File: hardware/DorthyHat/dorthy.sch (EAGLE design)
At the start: 25 parts, among them J1 90325-0004, J2 90325-0004, U2 DEV-15583

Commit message: added touch screen lcd to dorthy, realized teensy 4.0 does not have true analog outputs, need to revert to 3.5 if I want simple outs...
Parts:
- removed R7: 10k, rcl:R-US_R0805
- removed R8: 10K, rcl:R-US_R0805
- added R10, R11: 10K, rcl:R-US_0207/10
- added R9: 100, rcl:R-US_0207/10
- added SV7: (no value), con-lstb:MA04-1
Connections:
- new net LED: JP1.8, R9.2
- net GND: now also SV7.1
- net LA: no longer U2.15
- net RA: no longer U2.14
- net SCL: now also R10.2, SV7.4; no longer R7.2
- net SDA: now also R11.2, SV7.3; no longer R8.2
- net VCC: now also R9.1; no longer JP1.8
- net VEE: now also R10.1, R11.1, SV7.2; no longer R7.1, R8.1
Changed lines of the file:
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@@
 <part name="C3" library="capacitor-wima" library_urn="urn:adsk.eagle:library:116" deviceset="C" device="5/3.5" package3d_urn="urn:adsk.eagle:package:5427/1" value="1uf"/>
 <part name="U$7" library="seeedgrove" deviceset="110990030" device=""/>
-<part name="R7" library="rcl" library_urn="urn:adsk.eagle:library:334" deviceset="R-US_" device="R0805" package3d_urn="urn:adsk.eagle:package:23553/2" value="10k"/>
-<part name="R8" library="rcl" library_urn="urn:adsk.eagle:library:334" deviceset="R-US_" device="R0805" package3d_urn="urn:adsk.eagle:package:23553/2" value="10K"/>
 <part name="SV5" library="con-lstb" library_urn="urn:adsk.eagle:library:162" deviceset="MA04-1" device="" package3d_urn="urn:adsk.eagle:package:8337/1"/>
 <part name="SV2" library="con-lsta" library_urn="urn:adsk.eagle:library:161" deviceset="FE06-1" device="" package3d_urn="urn:adsk.eagle:package:8191/1"/>
@@
 <part name="U2" library="DEV-15583" deviceset="DEV-15583" device=""/>
 <part name="JP1" library="pinhead" library_urn="urn:adsk.eagle:library:325" deviceset="PINHD-1X14" device="" package3d_urn="urn:adsk.eagle:package:22417/2"/>
+<part name="R9" library="rcl" library_urn="urn:adsk.eagle:library:334" deviceset="R-US_" device="0207/10" package3d_urn="urn:adsk.eagle:package:23491/2" value="100"/>
+<part name="R10" library="rcl" library_urn="urn:adsk.eagle:library:334" deviceset="R-US_" device="0207/10" package3d_urn="urn:adsk.eagle:package:23491/2" value="10K"/>
+<part name="R11" library="rcl" library_urn="urn:adsk.eagle:library:334" deviceset="R-US_" device="0207/10" package3d_urn="urn:adsk.eagle:package:23491/2" value="10K"/>
+<part name="SV7" library="con-lstb" library_urn="urn:adsk.eagle:library:162" deviceset="MA04-1" device="" package3d_urn="urn:adsk.eagle:package:8337/1"/>
 </parts>
 <sheets>
@@
 <plain>
 <text x="157.48" y="81.28" size="1.778" layer="91">LCD Display</text>
-<text x="157.48" y="132.08" size="1.778" layer="91">Optional pullups, do not populate if not needed</text>
+<text x="154.94" y="134.62" size="1.778" layer="91">Optional pullups, do not populate if not needed</text>
 <text x="137.16" y="48.26" size="1.778" layer="91">Optional, connector if desired to go grove to grove. beware of orintation during install</text>
 <text x="-63.5" y="35.56" size="1.778" layer="91">MIDI THROUGH</text>
@@
 <attribute name="VALUE" x="162.56" y="71.12" size="1.27" layer="96"/>
 </instance>
-<instance part="R7" gate="G$1" x="177.8" y="127" smashed="yes">
-<attribute name="NAME" x="173.99" y="128.4986" size="1.778" layer="95"/>
-<attribute name="VALUE" x="173.99" y="123.698" size="1.778" layer="96"/>
-</instance>
-<instance part="R8" gate="G$1" x="177.8" y="119.38" smashed="yes">
-<attribute name="NAME" x="173.99" y="120.8786" size="1.778" layer="95"/>
-<attribute name="VALUE" x="173.99" y="116.078" size="1.778" layer="96"/>
-</instance>
 <instance part="SV5" gate="1" x="182.88" y="66.04" smashed="yes">
 <attribute name="VALUE" x="181.61" y="55.88" size="1.778" layer="96"/>
@@
 <attribute name="NAME" x="-52.07" y="145.415" size="1.778" layer="95"/>
 <attribute name="VALUE" x="-52.07" y="104.14" size="1.778" layer="96"/>
+</instance>
+<instance part="R9" gate="G$1" x="-114.3" y="121.92" smashed="yes">
+<attribute name="NAME" x="-113.03" y="125.9586" size="1.778" layer="95"/>
+<attribute name="VALUE" x="-113.03" y="123.698" size="1.778" layer="96"/>
+</instance>
+<instance part="R10" gate="G$1" x="177.8" y="127" smashed="yes">
+<attribute name="NAME" x="179.07" y="131.0386" size="1.778" layer="95"/>
+<attribute name="VALUE" x="179.07" y="128.778" size="1.778" layer="96"/>
+</instance>
+<instance part="R11" gate="G$1" x="177.8" y="119.38" smashed="yes">
+<attribute name="NAME" x="179.07" y="123.4186" size="1.778" layer="95"/>
+<attribute name="VALUE" x="179.07" y="121.158" size="1.778" layer="96"/>
+</instance>
+<instance part="SV7" gate="1" x="152.4" y="205.74" smashed="yes">
+<attribute name="VALUE" x="151.13" y="195.58" size="1.778" layer="96"/>
+<attribute name="NAME" x="151.13" y="211.582" size="1.778" layer="95"/>
 </instance>
 </instances>
@@
 </segment>
 <segment>
-<pinref part="JP1" gate="A" pin="8"/>
-<wire x1="-48.26" y1="124.46" x2="-60.96" y2="124.46" width="0.1524" layer="91"/>
-<label x="-60.96" y="124.46" size="1.778" layer="95"/>
+<pinref part="R9" gate="G$1" pin="1"/>
+<wire x1="-119.38" y1="121.92" x2="-129.54" y2="121.92" width="0.1524" layer="91"/>
+<label x="-127" y="121.92" size="1.778" layer="95"/>
 </segment>
 </net>
@@
 <wire x1="-48.26" y1="139.7" x2="-60.96" y2="139.7" width="0.1524" layer="91"/>
 <label x="-60.96" y="139.7" size="1.778" layer="95"/>
+</segment>
+<segment>
+<wire x1="177.8" y1="200.66" x2="160.02" y2="200.66" width="0.1524" layer="91"/>
+<label x="160.02" y="200.66" size="1.778" layer="95"/>
+<pinref part="SV7" gate="1" pin="1"/>
 </segment>
 </net>
@@
 <wire x1="167.64" y1="119.38" x2="172.72" y2="119.38" width="0.1524" layer="91"/>
 <label x="167.64" y="127" size="1.778" layer="95"/>
-<pinref part="R7" gate="G$1" pin="1"/>
-<pinref part="R8" gate="G$1" pin="1"/>
+<pinref part="R11" gate="G$1" pin="1"/>
+<pinref part="R10" gate="G$1" pin="1"/>
 </segment>
 <segment>
@@
 <label x="-60.96" y="134.62" size="1.778" layer="95"/>
 </segment>
+<segment>
+<wire x1="177.8" y1="203.2" x2="160.02" y2="203.2" width="0.1524" layer="91"/>
+<label x="160.02" y="203.2" size="1.778" layer="95"/>
+<pinref part="SV7" gate="1" pin="2"/>
+</segment>
 </net>
 <net name="RXBUF" class="0">
@@
 <wire x1="182.88" y1="127" x2="190.5" y2="127" width="0.1524" layer="91"/>
 <label x="185.42" y="127" size="1.778" layer="95"/>
-<pinref part="R7" gate="G$1" pin="2"/>
+<pinref part="R10" gate="G$1" pin="2"/>
 </segment>
 <segment>
@@
 <pinref part="U2" gate="G$1" pin="19"/>
 </segment>
+<segment>
+<wire x1="177.8" y1="208.28" x2="160.02" y2="208.28" width="0.1524" layer="91"/>
+<label x="160.02" y="208.28" size="1.778" layer="95"/>
+<pinref part="SV7" gate="1" pin="4"/>
+</segment>
 </net>
 <net name="SDA" class="0">
@@
 <wire x1="182.88" y1="119.38" x2="190.5" y2="119.38" width="0.1524" layer="91"/>
 <label x="185.42" y="119.38" size="1.778" layer="95"/>
-<pinref part="R8" gate="G$1" pin="2"/>
+<pinref part="R11" gate="G$1" pin="2"/>
 </segment>
 <segment>
@@
 <pinref part="U2" gate="G$1" pin="18"/>
 </segment>
+<segment>
+<wire x1="177.8" y1="205.74" x2="160.02" y2="205.74" width="0.1524" layer="91"/>
+<label x="160.02" y="205.74" size="1.778" layer="95"/>
+<pinref part="SV7" gate="1" pin="3"/>
+</segment>
 </net>
 <net name="MIDITX" class="0">
@@
 </segment>
 <segment>
-<wire x1="33.02" y1="121.92" x2="43.18" y2="121.92" width="0.1524" layer="91"/>
-<label x="35.56" y="121.92" size="1.778" layer="95"/>
-<pinref part="U2" gate="G$1" pin="15"/>
+<wire x1="12.7" y1="160.02" x2="22.86" y2="160.02" width="0.1524" layer="91"/>
+<label x="15.24" y="160.02" size="1.778" layer="95"/>
 </segment>
 </net>
@@
 </segment>
 <segment>
-<wire x1="33.02" y1="119.38" x2="43.18" y2="119.38" width="0.1524" layer="91"/>
-<label x="35.56" y="119.38" size="1.778" layer="95"/>
-<pinref part="U2" gate="G$1" pin="14"/>
+<wire x1="12.7" y1="157.48" x2="22.86" y2="157.48" width="0.1524" layer="91"/>
+<label x="15.24" y="157.48" size="1.778" layer="95"/>
 </segment>
 </net>
@@
 </segment>
 </net>
+<net name="LED" class="0">
+<segment>
+<pinref part="JP1" gate="A" pin="8"/>
+<wire x1="-48.26" y1="124.46" x2="-60.96" y2="124.46" width="0.1524" layer="91"/>
+<label x="-60.96" y="124.46" size="1.778" layer="95"/>
+</segment>
+<segment>
+<pinref part="R9" gate="G$1" pin="2"/>
+<wire x1="-109.22" y1="121.92" x2="-96.52" y2="121.92" width="0.1524" layer="91"/>
+<label x="-106.68" y="121.92" size="1.778" layer="95"/>
+</segment>
+</net>

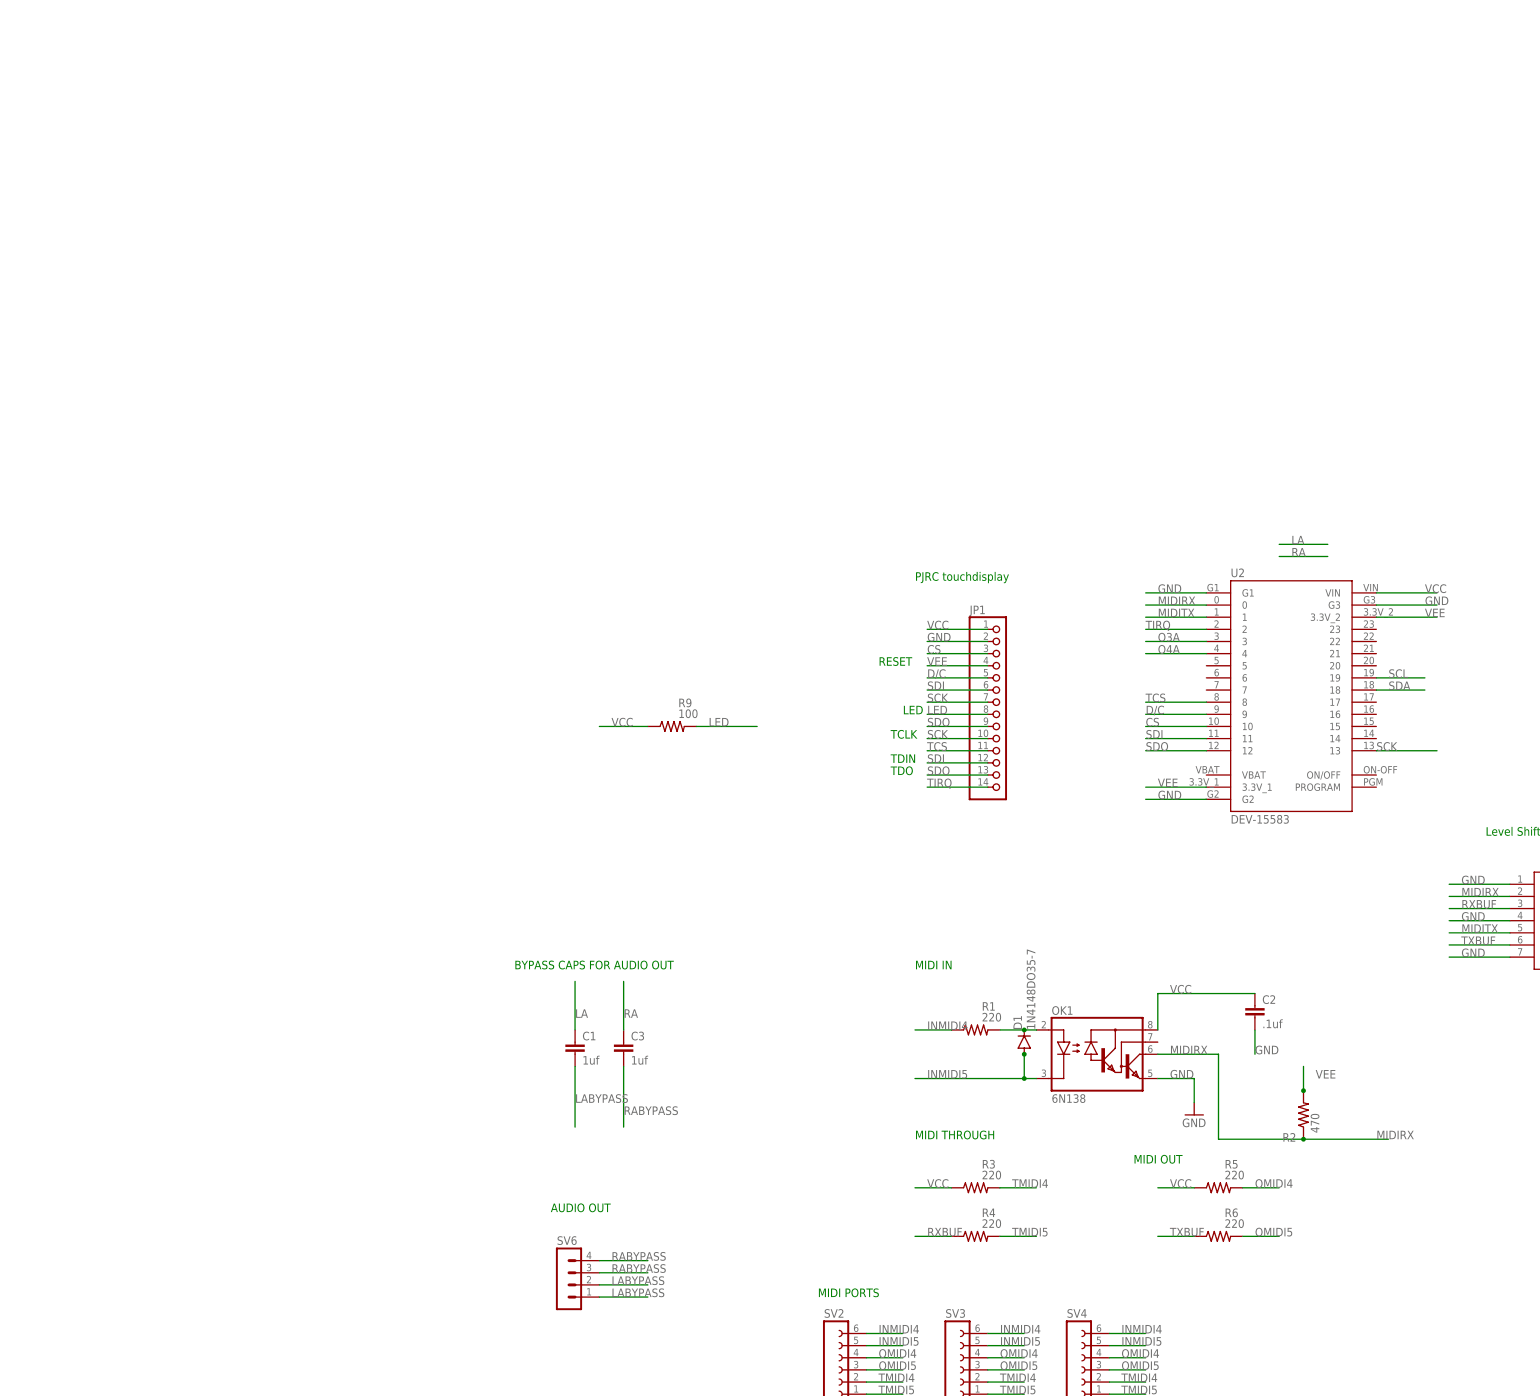
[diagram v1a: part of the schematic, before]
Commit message: change to teensy 3.6. Add AGND for audio outs. Add power headers for future addons
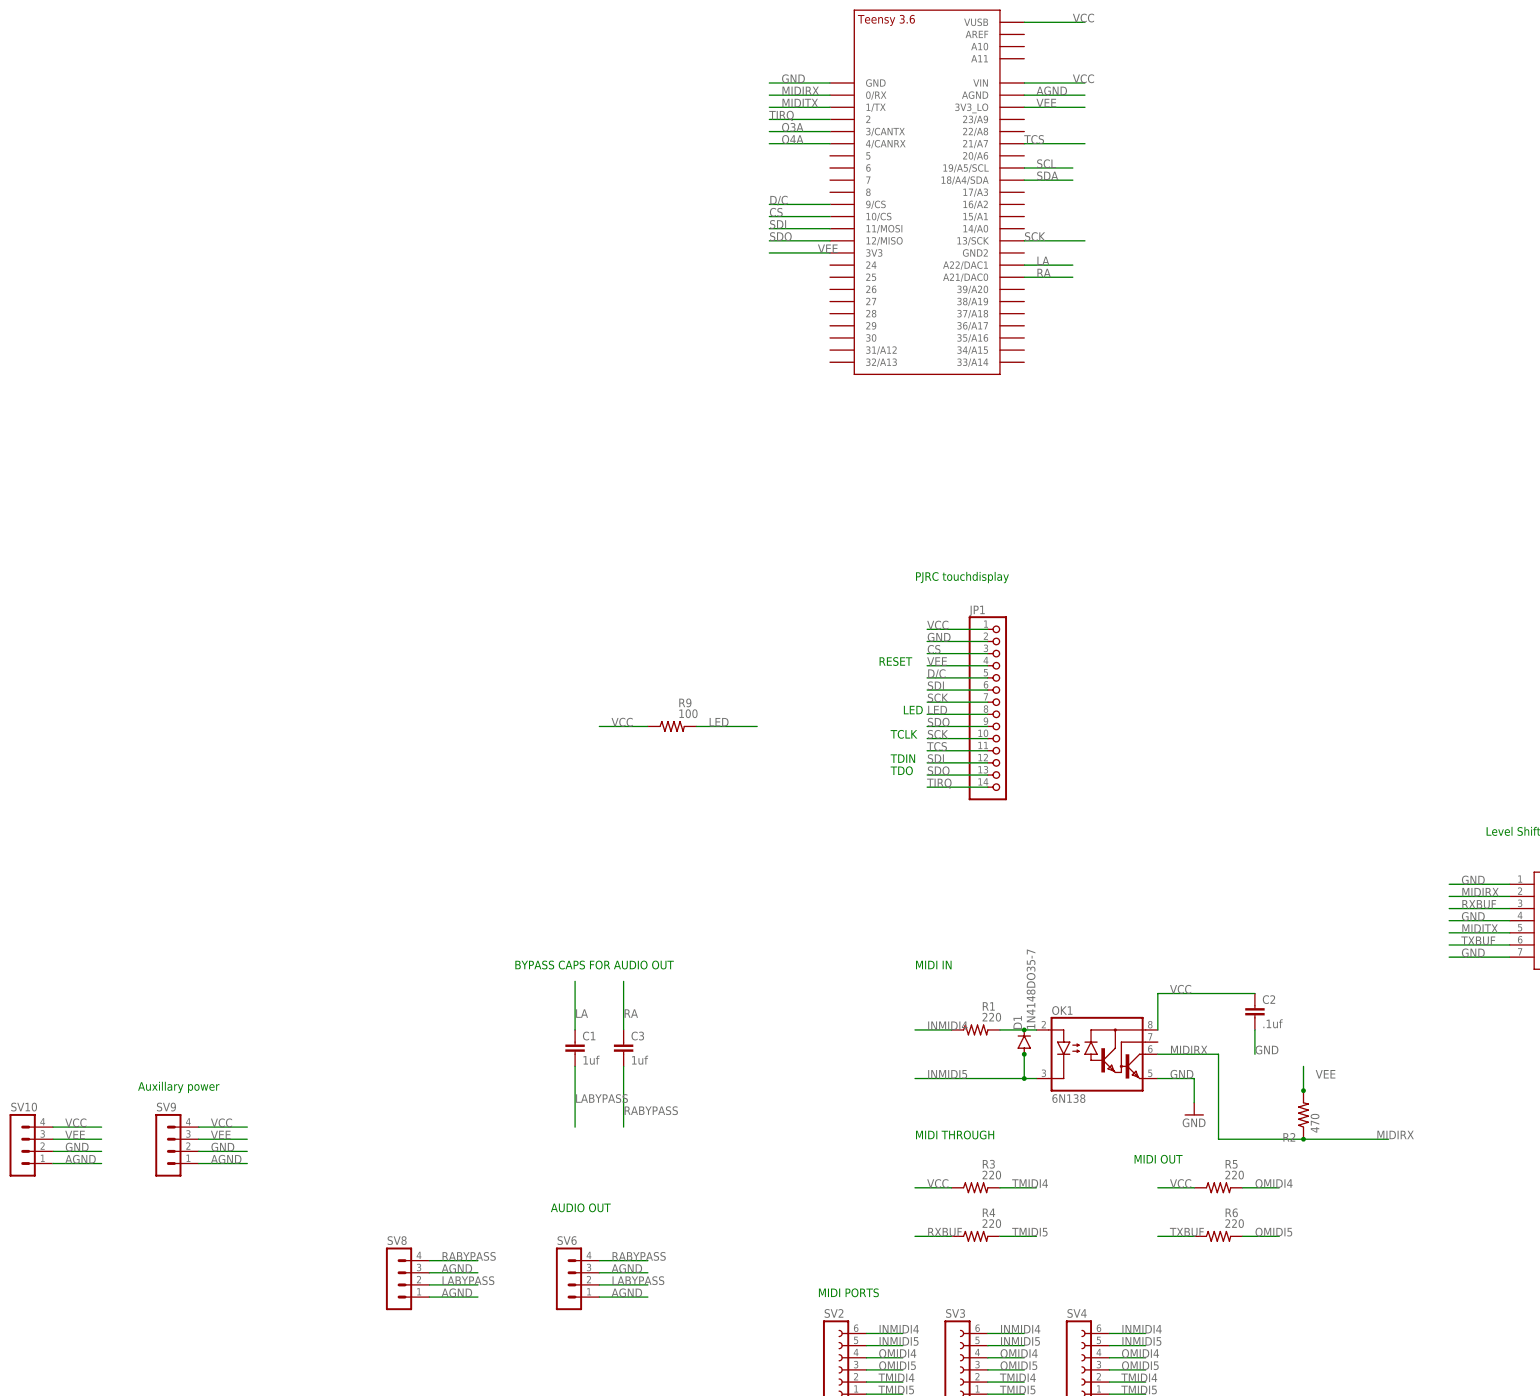
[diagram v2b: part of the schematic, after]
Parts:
- removed U2: DEV-15583, DEV-15583:DEV-15583
- added SV10, SV8, SV9: (no value), con-lstb:MA04-1
- added U$1: TEENSY_3.5/3.6_BASIC, Teensy356:TEENSY_3.5/3.6_BASIC
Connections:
- new net AGND: SV10.1, SV6.1, SV6.3, SV8.1, SV8.3, SV9.1, U$1.AGND
- net CS: now also U$1.10/CS; no longer U2.10
- net D/C: now also U$1.9/CS; no longer U2.9
- net GND: now also SV10.2, SV9.2, U$1.GND; no longer U2.G1, U2.G2, U2.G3
- net LA: now also U$1.A22/DAC1
- net LABYPASS: now also SV8.2; no longer SV6.1
- net MIDIRX: now also U$1.0/RX; no longer U2.0
- net MIDITX: now also U$1.1/TX; no longer U2.1
- net O3A: now also U$1.3/CANTX; no longer U2.3
- net O4A: now also U$1.4/CANRX; no longer U2.4
- net RA: now also U$1.A21/DAC0
- net RABYPASS: now also SV8.4; no longer SV6.3
- net SCK: now also U$1.13/SCK; no longer U2.13
- net SCL: now also U$1.19/A5/SCL; no longer U2.19
- net SDA: now also U$1.18/A4/SDA; no longer U2.18
- net SDI: now also U$1.11/MOSI; no longer U2.11
- net SDO: now also U$1.12/MISO; no longer U2.12
- net TCS: now also U$1.21/A7; no longer U2.8
- net TIRQ: now also U$1.2; no longer U2.2
- net VCC: now also SV10.4, SV9.4, U$1.VIN, U$1.VUSB; no longer U2.VIN
- net VEE: now also SV10.3, SV9.3, U$1.3V3, U$1.3V3_LO; no longer U2.3.3V_1, U2.3.3V_2
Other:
- note added: "Auxillary power"

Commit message: make board 100mmX100mm. add 9 capacitive touch pads. add rotary encoder... why not?
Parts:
- added MT1: PEC11R-4215F-S0024, PEC11R-4215F-S0024:PEC11R-4215F-S0024
- added TP$1, TP$2, TP$3, TP$4, TP$5, TP$6, TP$7, TP$8, TP$9: CAPACITIVE_TOUCH_PAD, CRcustom:CAPACITIVE_TOUCH_PAD
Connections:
- new net EA: MT1.A, U$1.6
- new net EB: MT1.B, U$1.7
- new net P1: TP$1.P$1, U$1.23/A9
- new net P2: TP$2.P$1, U$1.22/A8
- new net P3: TP$3.P$1, U$1.17/A3
- new net P4: TP$4.P$1, U$1.16/A2
- new net P5: TP$5.P$1, U$1.15/A1
- new net P6: TP$6.P$1, U$1.29
- new net P7: TP$7.P$1, U$1.30
- new net P8: TP$8.P$1, U$1.19/A5/SCL
- new net P9: TP$9.P$1, U$1.18/A4/SDA
- new net SW1: MT1.1, U$1.5
- net GND: now also MT1.2, MT1.COM, MT1.SHIELD
- net O3A: no longer U$1.3/CANTX
- net O4A: no longer U$1.4/CANRX
- net SCL: now also U$1.3/CANTX; no longer U$1.19/A5/SCL
- net SDA: now also U$1.4/CANRX; no longer U$1.18/A4/SDA
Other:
- note added: "Rotary Encoder"
- note added: "TOUCH PADS"
- note added: "touch"
- moved on the sheet: C1, C3, R9, SV10, SV5, SV6, SV8, SV9, U$7
